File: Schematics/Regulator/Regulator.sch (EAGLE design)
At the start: 28 parts, among them IC1 LM317BD2T, IC2 LM337_D2PAC

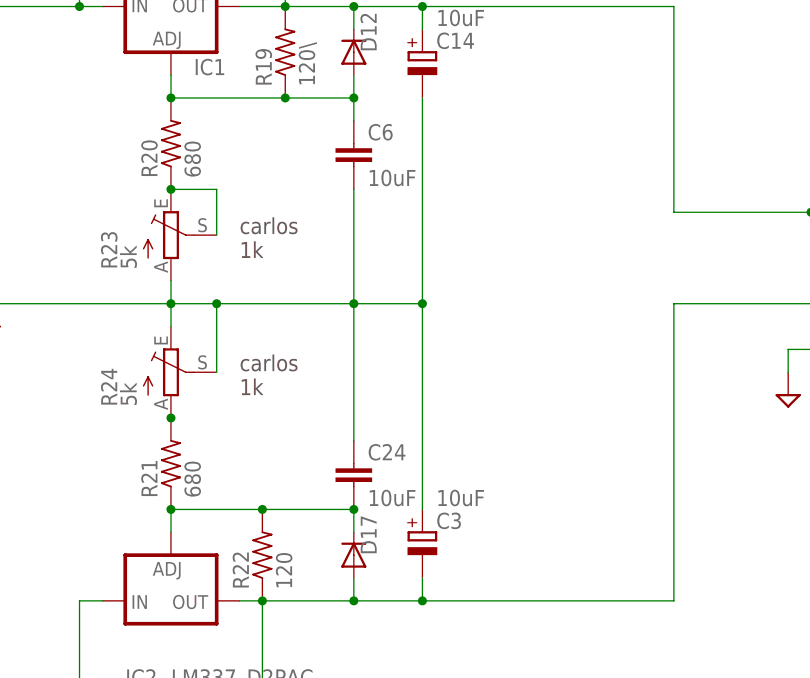
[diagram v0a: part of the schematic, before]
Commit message: updated gerbers for regulator board
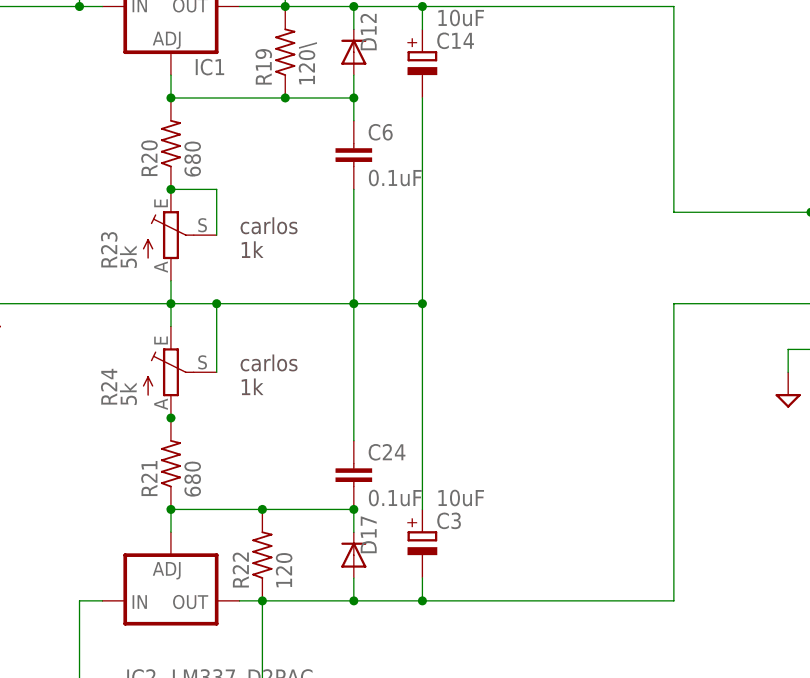
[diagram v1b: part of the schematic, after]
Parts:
- C24, C6: value 10uF -> 0.1uF
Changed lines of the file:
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@@
 <part name="R19" library="rcl" deviceset="R-US_" device="0309/V" value="120\"/>
 <part name="R20" library="rcl" deviceset="R-US_" device="0309/V" value="680"/>
-<part name="C6" library="resistor" deviceset="C-EU" device="025-025X050" value="10uF"/>
+<part name="C6" library="resistor" deviceset="C-EU" device="025-025X050" value="0.1uF"/>
 <part name="SGND2" library="supply2" deviceset="GND5" device="" value="SGND"/>
 <part name="C18" library="rcl" deviceset="C-EU" device="025-025X050" value="1nF"/>
@@
 <part name="R22" library="rcl" deviceset="R-US_" device="0309/V" value="120"/>
 <part name="D17" library="Amplifier_Parts" deviceset="1N4004" device=""/>
-<part name="C24" library="resistor" deviceset="C-EU" device="025-025X050" value="10uF"/>
+<part name="C24" library="resistor" deviceset="C-EU" device="025-025X050" value="0.1uF"/>
 <part name="D18" library="Amplifier_Parts" deviceset="1N4004" device=""/>
 <part name="C14" library="rcl" deviceset="CPOL-EU" device="E2.5-6" value="10uF"/>
